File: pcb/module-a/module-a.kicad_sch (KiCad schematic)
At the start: 37 parts, among them J1 Conn_01x06, J2 Conn_01x06, SW1 SW_Push, SW10 SW_Push, SW11 SW_Push, SW12 SW_Push, SW2 SW_Push, SW3 SW_Push, SW4 SW_Push, SW5 SW_Push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

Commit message: Add module-0 board
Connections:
- net ~{MCP_RST}: now reaches U1.11 (IO7), U2.18 (~{RESET})
- net ~{CS} renamed ~{MCP_CS}
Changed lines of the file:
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@@
+		)
+	)
+	(label "~{MCP_RST}"
+		(at 170.18 83.82 0)
+		(effects
+			(font
+				(size 1.27 1.27)
+			)
+			(justify left bottom)
 		)
 	)
@@
 		)
 	)
-	(label "~{CS}"
+	(label "~{MCP_CS}"
 		(at 104.14 80.01 0)
 		(effects

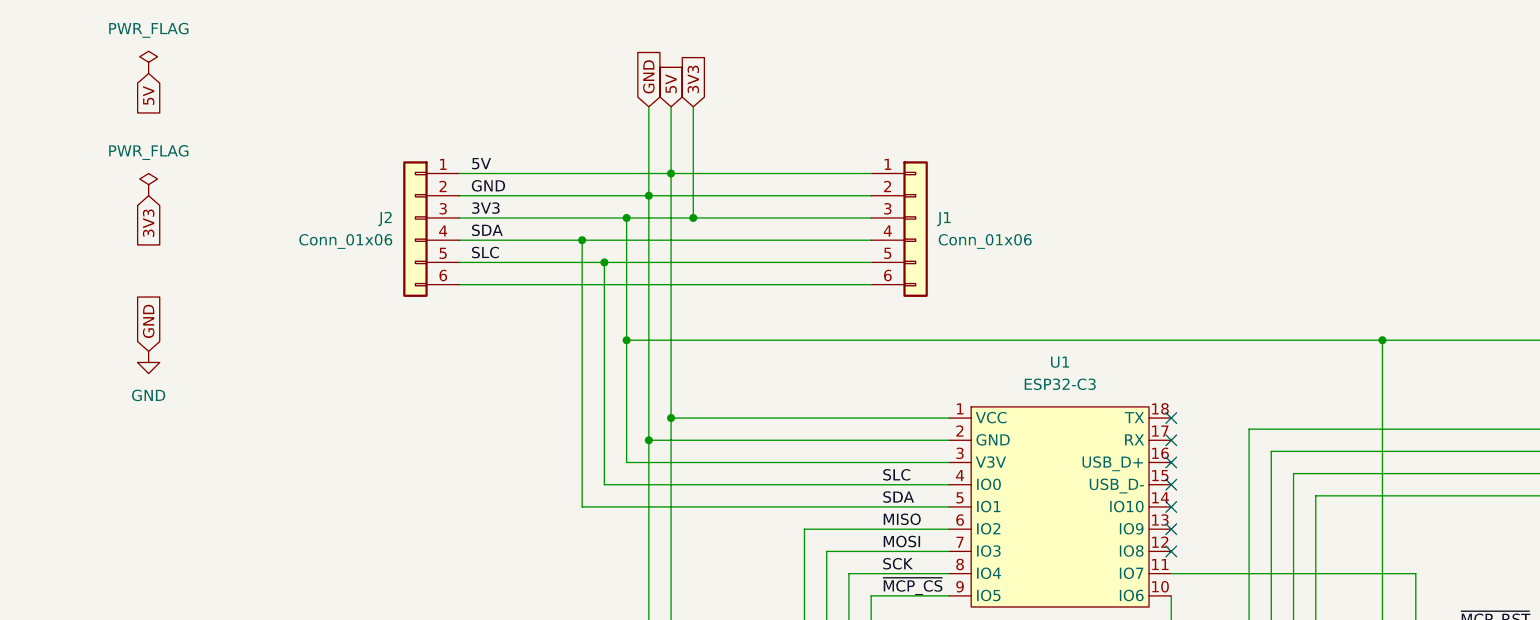
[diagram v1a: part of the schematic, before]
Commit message: 3V net should not be shared across the bus
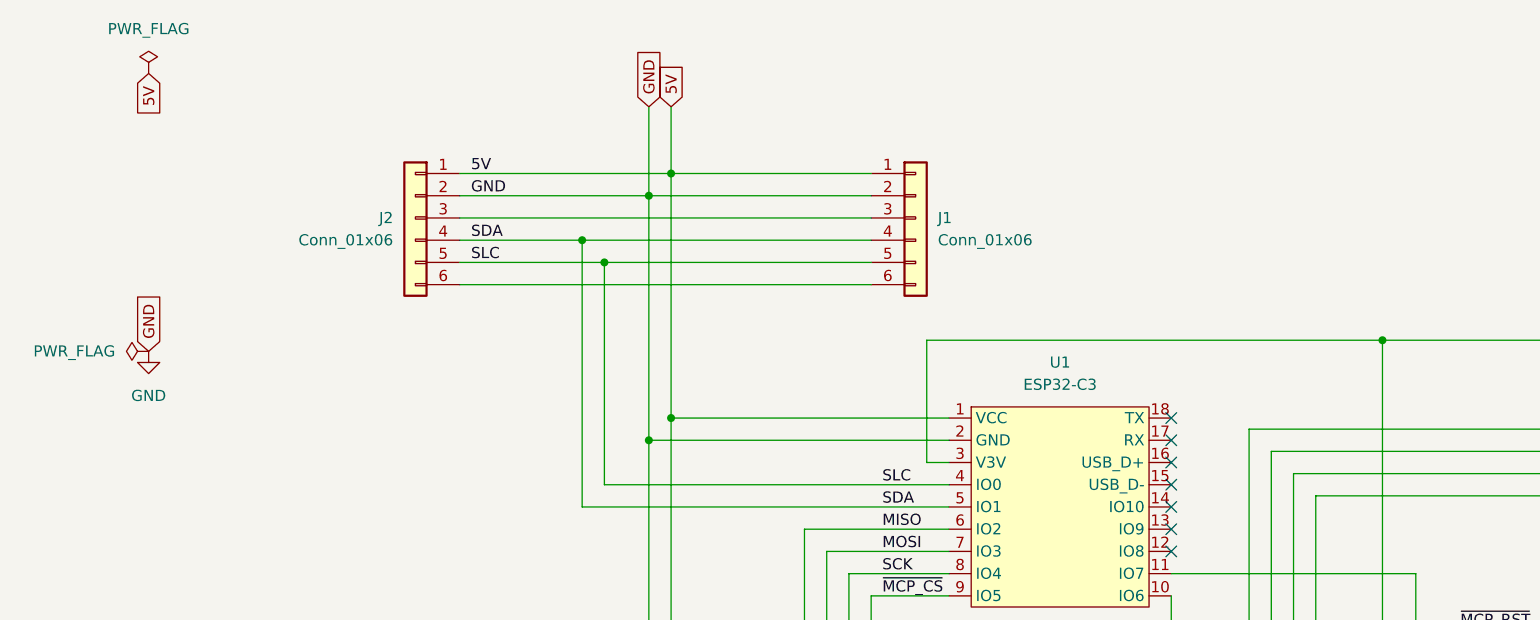
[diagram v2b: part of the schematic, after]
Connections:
- net 3V3: no longer names the net of C1.1, U1.3 (V3V), U2.9 (VDD)
- net 3V3: no longer J1.3 (Pin_3), J2.3 (Pin_3)
- new net: J1.3 (Pin_3), J2.3 (Pin_3)
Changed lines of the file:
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@@
 	)
 	(junction
-		(at 74.93 50.8)
-		(diameter 0)
-		(color 0 0 0 0)
-	)
-	(junction
 		(at 139.7 163.83)
 		(diameter 0)
@@
 	)
 	(junction
-		(at 74.93 36.83)
-		(diameter 0)
-		(color 0 0 0 0)
-	)
-	(junction
 		(at 379.73 50.8)
 		(diameter 0)
@@
 	)
 	(junction
-		(at 82.55 36.83)
-		(diameter 0)
-		(color 0 0 0 0)
-	)
-	(junction
 		(at 306.07 154.94)
 		(diameter 0)
@@
 	(wire
 		(pts
-			(xy 55.88 36.83) (xy 74.93 36.83)
-		)
-		(stroke
-			(width 0)
-			(type default)
-		)
-	)
-	(wire
-		(pts
 			(xy 238.76 139.7) (xy 273.05 139.7)
 		)
@@
 	(wire
 		(pts
-			(xy 82.55 36.83) (xy 102.87 36.83)
+			(xy 55.88 36.83) (xy 102.87 36.83)
 		)
 		(stroke
@@
 	(wire
 		(pts
-			(xy 74.93 64.77) (xy 111.76 64.77)
+			(xy 109.22 64.77) (xy 111.76 64.77)
 		)
 		(stroke
@@
 	(wire
 		(pts
-			(xy 74.93 64.77) (xy 74.93 50.8)
+			(xy 109.22 64.77) (xy 109.22 50.8)
 		)
 		(stroke
@@
 	(wire
 		(pts
-			(xy 74.93 50.8) (xy 161.29 50.8)
+			(xy 109.22 50.8) (xy 161.29 50.8)
 		)
 		(stroke
@@
 	(wire
 		(pts
-			(xy 82.55 24.13) (xy 82.55 36.83)
-		)
-		(stroke
-			(width 0)
-			(type default)
-		)
-	)
-	(wire
-		(pts
 			(xy 198.12 139.7) (xy 198.12 170.18)
 		)
@@
 	(wire
 		(pts
-			(xy 74.93 36.83) (xy 82.55 36.83)
-		)
-		(stroke
-			(width 0)
-			(type default)
-		)
-	)
-	(wire
-		(pts
 			(xy 238.76 170.18) (xy 273.05 170.18)
 		)
@@
 	(wire
 		(pts
-			(xy 74.93 36.83) (xy 74.93 50.8)
-		)
-		(stroke
-			(width 0)
-			(type default)
-		)
-	)
-	(wire
-		(pts
 			(xy 161.29 113.03) (xy 77.47 113.03)
 		)
@@
 		)
 	)
-	(label "3V3"
-		(at 57.15 36.83 0)
-		(effects
-			(font
-				(size 1.27 1.27)
-			)
-			(justify left bottom)
-		)
-	)
 	(label "SDA"
 		(at 57.15 39.37 0)
@@
 		)
 	)
-	(global_label "3V3"
-		(shape input)
-		(at 82.55 24.13 90)
-		(fields_autoplaced yes)
-		(effects
-			(font
-				(size 1.27 1.27)
-			)
-			(justify left)
-		)
-		(property "Intersheetrefs" "${INTERSHEET_REFS}"
-			(at 82.55 17.6372 90)
-			(effects
-				(font
-					(size 1.27 1.27)
-				)
-				(justify left)
-				(hide yes)
-			)
-		)
-	)
-	(global_label "3V3"
-		(shape input)
-		(at 20.32 34.29 270)
-		(fields_autoplaced yes)
-		(effects
-			(font
-				(size 1.27 1.27)
-			)
-			(justify right)
-		)
-		(property "Intersheetrefs" "${INTERSHEET_REFS}"
-			(at 20.32 40.7828 90)
-			(effects
-				(font
-					(size 1.27 1.27)
-				)
-				(justify right)
-				(hide yes)
-			)
-		)
-	)
 	(global_label "GND"
 		(shape input)
@@
 	)
 	(symbol
-		(lib_id "power:PWR_FLAG")
-		(at 20.32 34.29 0)
-		(unit 1)
-		(exclude_from_sim no)
-		(in_bom yes)
-		(on_board yes)
-		(dnp no)
-		(fields_autoplaced yes)
-		(property "Reference" "#FLG02"
-			(at 20.32 32.385 0)
-			(effects
-				(font
-					(size 1.27 1.27)
-				)
-				(hide yes)
-			)
-		)
-		(property "Value" "PWR_FLAG"
-			(at 20.32 29.21 0)
-			(effects
-				(font
-					(size 1.27 1.27)
-				)
-			)
-		)
-		(property "Footprint" ""
-			(at 20.32 34.29 0)
-			(effects
-				(font
-					(size 1.27 1.27)
-				)
-				(hide yes)
-			)
-		)
-		(property "Datasheet" "~"
-			(at 20.32 34.29 0)
-			(effects
-				(font
-					(size 1.27 1.27)
-				)
-				(hide yes)
-			)
-		)
-		(property "Description" "Special symbol for telling ERC where power comes from"
-			(at 20.32 34.29 0)
-			(effects
-				(font
-					(size 1.27 1.27)
-				)
-				(hide yes)
-			)
-		)
-		(pin "1"
-		)
-		(instances
-			(project "modular-key-pad"
-				(path "/0888bf04-c6c1-4923-af80-2189ee3798b4"
-					(reference "#FLG02")
-					(unit 1)
-				)
-			)
-		)
-	)
-	(symbol
 		(lib_id "Switch:SW_Push")
 		(at 394.97 55.88 270)
@@
 					(unit 1)
 				)
+			)
+		)
+	)
+	(symbol
+		(lib_id "power:PWR_FLAG")
+		(at 20.32 52.07 90)
+		(unit 1)
+		(exclude_from_sim no)
+		(in_bom yes)
+		(on_board yes)
+		(dnp no)
+		(fields_autoplaced yes)
+		(property "Reference" "#FLG03"
+			(at 18.415 52.07 0)
+			(effects
+				(font
+					(size 1.27 1.27)
+				)
+				(hide yes)
+			)
+		)
+		(property "Value" "PWR_FLAG"
+			(at 16.51 52.0699 90)
+			(effects
+				(font
+					(size 1.27 1.27)
+				)
+				(justify left)
+			)
+		)
+		(property "Footprint" ""
+			(at 20.32 52.07 0)
+			(effects
+				(font
+					(size 1.27 1.27)
+				)
+				(hide yes)
+			)
+		)
+		(property "Datasheet" "~"
+			(at 20.32 52.07 0)
+			(effects
+				(font
+					(size 1.27 1.27)
+				)
+				(hide yes)
+			)
+		)
+		(property "Description" "Special symbol for telling ERC where power comes from"
+			(at 20.32 52.07 0)
+			(effects
+				(font
+					(size 1.27 1.27)
+				)
+				(hide yes)
+			)
+		)
+		(pin "1"
+		)
+		(instances
+			(project "module-a"
+				(path "/0888bf04-c6c1-4923-af80-2189ee3798b4"
+					(reference "#FLG03")
+					(unit 1)
+				)

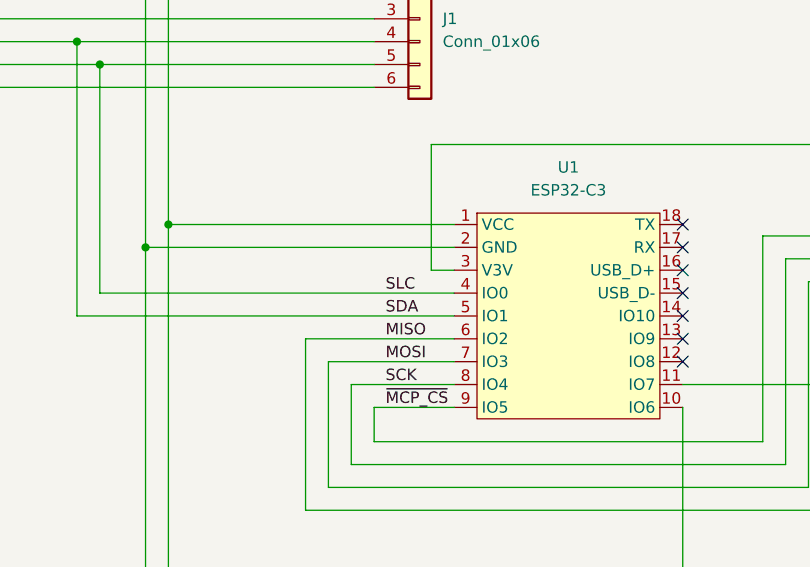
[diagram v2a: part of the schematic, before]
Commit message: Refactor firmware construction
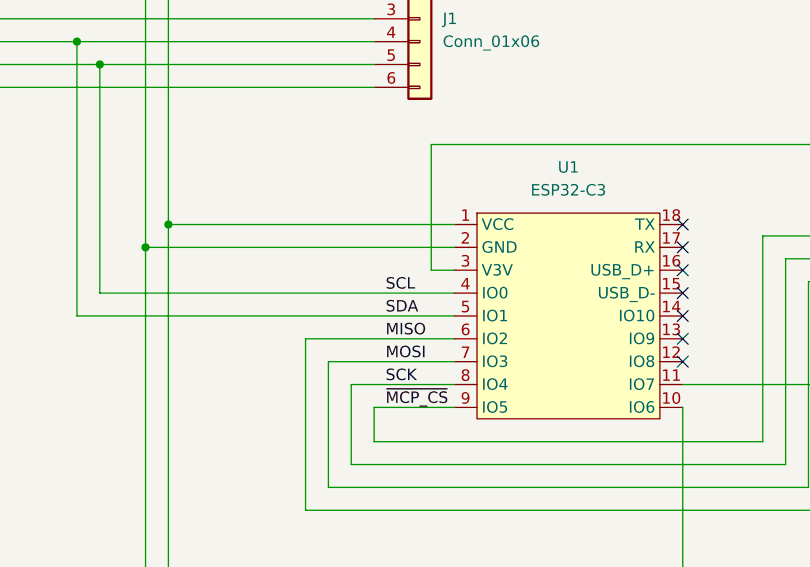
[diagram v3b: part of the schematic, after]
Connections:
- net SLC renamed SCL
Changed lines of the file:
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@@
 		)
 	)
-	(label "SLC"
+	(label "SCL"
 		(at 104.14 67.31 0)
 		(effects
